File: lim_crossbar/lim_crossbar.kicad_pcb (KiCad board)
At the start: 4 copper layers, 166 x 19 mm, 13 parts, among them J1 Conn_02x12_Counter_Clockwise, J2 Conn_02x12_Counter_Clockwise, J3 Conn_02x12_Counter_Clockwise, J4 Conn_02x08_Odd_Even, J5 Conn_02x08_Odd_Even

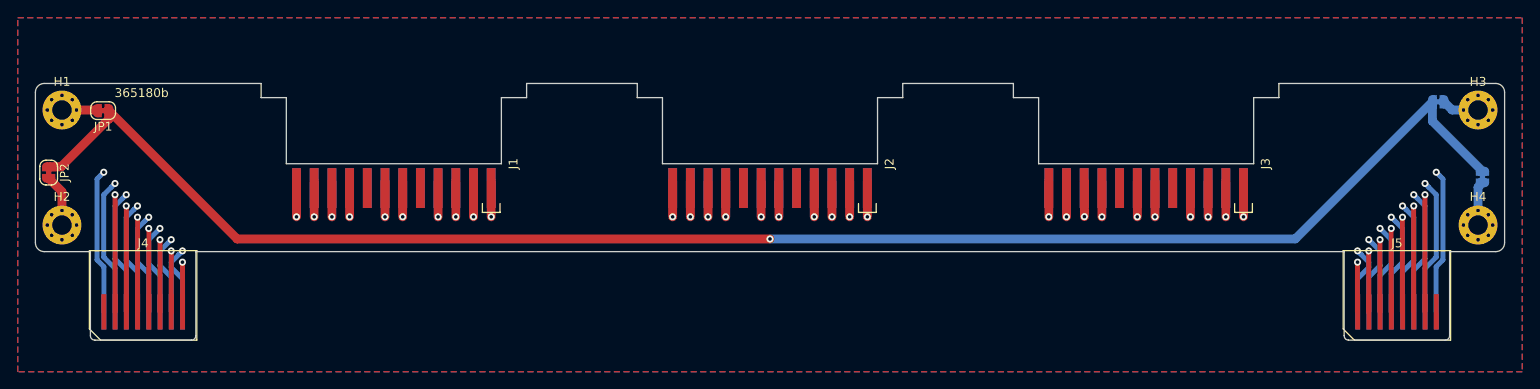
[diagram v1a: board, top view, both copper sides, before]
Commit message: otter crossbars shortened
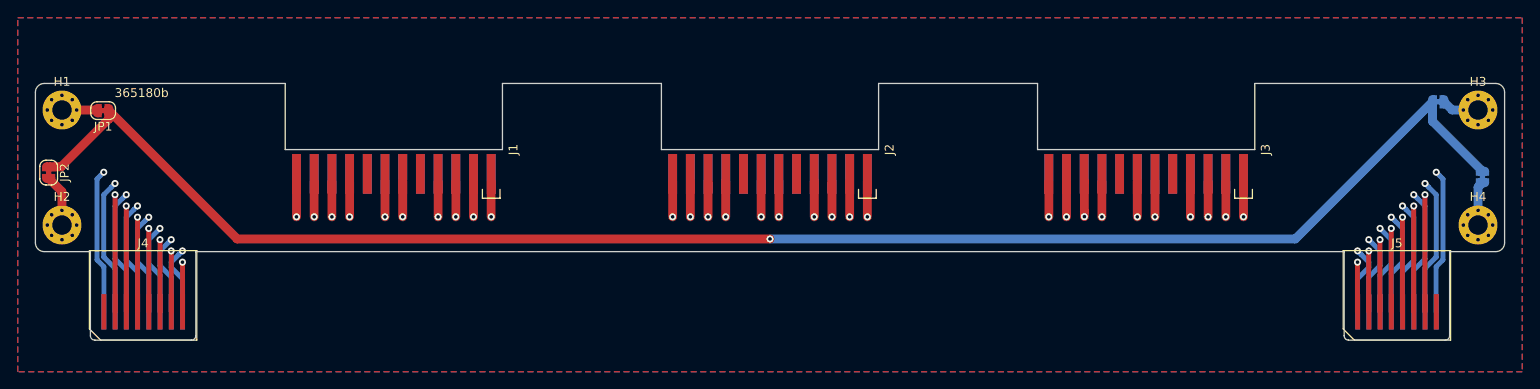
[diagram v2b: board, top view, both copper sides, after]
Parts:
- moved J1 1.60 mm to (-42.5, -21.5)
- moved J2 1.60 mm to (0.00, -21.5)
- moved J3 1.60 mm to (42.5, -21.5)
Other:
- outline, holes or cut-outs redrawn
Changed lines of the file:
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@@
-(kicad_pcb (version 20171130) (host pcbnew 5.1.5-rc1)
+(kicad_pcb (version 20171130) (host pcbnew 5.1.5)
   (general
     (thickness 1.6)
-    (drawings 33)
+    (drawings 23)
     (tracks 379)
     (zones 0)
@@
     (pad_to_mask_clearance 0.051)
     (solder_mask_min_width 0.25)
-    (aux_axis_origin 0 -21.43)
-    (grid_origin 0 -21.43)
+    (aux_axis_origin 0 -29)
+    (grid_origin 0 -29)
     (visible_elements FFFFFFFF)
     (pcbplotparams
@@
   )
   (module custom:PinSocket_2x12_P2.00mm_Vertical_EDGE (layer F.Cu)
-    (at 0 -19.93)
+    (at 0 -21.53)
     (descr "edge-mounted straight socket strip, 2x12, 2.00mm pitch, double cols (from Kicad 4.0.7), SQT-112-03-L-D")
     (tags "Edge mounted socket strip EDGE 2x12 2.00mm double row")
@@
     (fp_line (start 12 5.5) (end 10 5.5) (layer F.SilkS) (width 0.15))
     (fp_line (start 12 4.5) (end 12 5.5) (layer F.SilkS) (width 0.15))
-    (fp_line (start 12.15 0) (end -12.15 0) (layer Edge.Cuts) (width 0.12))
+    (fp_line (start 12.27 0) (end -12.27 0) (layer Edge.Cuts) (width 0.12))
     (fp_line (start 12.15 0.25) (end -12.15 0.25) (layer B.Fab) (width 0.12))
     (fp_line (start 12.15 0.25) (end -12.15 0.25) (layer F.Fab) (width 0.12))
@@
   )
   (module custom:PinSocket_2x12_P2.00mm_Vertical_EDGE (layer F.Cu)
-    (at -42.5 -19.93)
+    (at -42.5 -21.53)
     (descr "edge-mounted straight socket strip, 2x12, 2.00mm pitch, double cols (from Kicad 4.0.7), SQT-112-03-L-D")
     (tags "Edge mounted socket strip EDGE 2x12 2.00mm double row")
@@
     (fp_line (start 12 5.5) (end 10 5.5) (layer F.SilkS) (width 0.15))
     (fp_line (start 12 4.5) (end 12 5.5) (layer F.SilkS) (width 0.15))
-    (fp_line (start 12.15 0) (end -12.15 0) (layer Edge.Cuts) (width 0.12))
+    (fp_line (start 12.27 0) (end -12.27 0) (layer Edge.Cuts) (width 0.12))
     (fp_line (start 12.15 0.25) (end -12.15 0.25) (layer B.Fab) (width 0.12))
     (fp_line (start 12.15 0.25) (end -12.15 0.25) (layer F.Fab) (width 0.12))
@@
   )
   (module custom:PinSocket_2x12_P2.00mm_Vertical_EDGE (layer F.Cu)
-    (at 42.5 -19.93)
+    (at 42.5 -21.53)
     (descr "edge-mounted straight socket strip, 2x12, 2.00mm pitch, double cols (from Kicad 4.0.7), SQT-112-03-L-D")
     (tags "Edge mounted socket strip EDGE 2x12 2.00mm double row")
@@
     (fp_line (start 12 5.5) (end 10 5.5) (layer F.SilkS) (width 0.15))
     (fp_line (start 12 4.5) (end 12 5.5) (layer F.SilkS) (width 0.15))
-    (fp_line (start 12.15 0) (end -12.15 0) (layer Edge.Cuts) (width 0.12))
+    (fp_line (start 12.27 0) (end -12.27 0) (layer Edge.Cuts) (width 0.12))
     (fp_line (start 12.15 0.25) (end -12.15 0.25) (layer B.Fab) (width 0.12))
     (fp_line (start 12.15 0.25) (end -12.15 0.25) (layer F.Fab) (width 0.12))
@@
       ))
   )
+  (gr_line (start 54.77 -21.53) (end 54.77 -29) (layer Edge.Cuts) (width 0.05))
+  (gr_line (start 30.23 -21.53) (end 30.23 -29) (layer Edge.Cuts) (width 0.05))
+  (gr_line (start 12.27 -21.53) (end 12.27 -29) (layer Edge.Cuts) (width 0.05))
+  (gr_line (start -30.23 -21.53) (end -30.23 -29) (layer Edge.Cuts) (width 0.05))
+  (gr_line (start -54.77 -21.53) (end -54.77 -29) (layer Edge.Cuts) (width 0.05))
+  (gr_line (start -12.27 -29) (end -30.23 -29) (layer Edge.Cuts) (width 0.05))
+  (gr_line (start -12.27 -21.53) (end -12.27 -29) (layer Edge.Cuts) (width 0.05))
+  (gr_line (start -87 2.5) (end 89 2.5) (layer Dwgs.User) (width 0.15))
+  (gr_line (start -87 -9.5) (end 89 -9.5) (layer Dwgs.User) (width 0.15))
   (gr_text 365180b (at -71 -27.93) (layer B.SilkS)
     (effects (font (size 1 1) (thickness 0.15)) (justify mirror))
@@
   (gr_arc (start 82 -11) (end 82 -10) (angle -90) (layer Edge.Cuts) (width 0.05))
   (gr_line (start 83 -11) (end 83 -28) (layer Edge.Cuts) (width 0.05))
-  (gr_line (start -57.5 -29) (end -82 -29) (layer Edge.Cuts) (width 0.05))
-  (gr_line (start -15 -29) (end -27.5 -29) (layer Edge.Cuts) (width 0.05))
-  (gr_line (start 27.5 -29) (end 15 -29) (layer Edge.Cuts) (width 0.05))
-  (gr_line (start 82 -29) (end 57.5 -29) (layer Edge.Cuts) (width 0.05))
-  (gr_line (start -30.35 -27.4) (end -27.5 -27.4) (layer Edge.Cuts) (width 0.05))
-  (gr_line (start -54.65 -19.93) (end -54.65 -27.4) (layer Edge.Cuts) (width 0.05))
-  (gr_line (start -27.5 -27.4) (end -27.5 -29) (layer Edge.Cuts) (width 0.05))
-  (gr_line (start -30.35 -19.93) (end -30.35 -27.4) (layer Edge.Cuts) (width 0.05))
-  (gr_line (start -57.5 -27.4) (end -57.5 -29) (layer Edge.Cuts) (width 0.05))
-  (gr_line (start -57.5 -27.4) (end -54.65 -27.4) (layer Edge.Cuts) (width 0.05))
-  (gr_line (start 54.65 -27.4) (end 57.5 -27.4) (layer Edge.Cuts) (width 0.05))
-  (gr_line (start 30.35 -19.93) (end 30.35 -27.4) (layer Edge.Cuts) (width 0.05))
-  (gr_line (start 57.5 -27.4) (end 57.5 -29) (layer Edge.Cuts) (width 0.05))
-  (gr_line (start 54.65 -19.93) (end 54.65 -27.4) (layer Edge.Cuts) (width 0.05))
-  (gr_line (start 27.5 -27.4) (end 27.5 -29) (layer Edge.Cuts) (width 0.05))
-  (gr_line (start 27.5 -27.4) (end 30.35 -27.4) (layer Edge.Cuts) (width 0.05))
-  (gr_line (start -15 -27.4) (end -15 -29) (layer Edge.Cuts) (width 0.05))
-  (gr_line (start 15 -27.4) (end 15 -29) (layer Edge.Cuts) (width 0.05))
-  (gr_line (start 12.15 -27.4) (end 15 -27.4) (layer Edge.Cuts) (width 0.05))
-  (gr_line (start 12.15 -19.93) (end 12.15 -27.4) (layer Edge.Cuts) (width 0.05))
-  (gr_line (start -15 -27.4) (end -12.15 -27.4) (layer Edge.Cuts) (width 0.05))
-  (gr_line (start -12.15 -19.93) (end -12.15 -27.4) (layer Edge.Cuts) (width 0.05))
+  (gr_line (start -54.77 -29) (end -82 -29) (layer Edge.Cuts) (width 0.05))
+  (gr_line (start 30.23 -29) (end 12.27 -29) (layer Edge.Cuts) (width 0.05))
+  (gr_line (start 82 -29) (end 54.77 -29) (layer Edge.Cuts) (width 0.05))
   (gr_arc (start 82 -28) (end 83 -28) (angle -90) (layer Edge.Cuts) (width 0.05))
   (gr_arc (start -82 -28) (end -82 -29) (angle -90) (layer Edge.Cuts) (width 0.05))

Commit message: update silk
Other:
- board text added: "6c4861d"
- board text removed: "365180b"
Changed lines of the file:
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@@
       (padsonsilk false)
       (subtractmaskfromsilk false)
-      (outputformat 3)
+      (outputformat 1)
       (mirror false)
       (drillshape 0)
@@
   (gr_line (start -87 2.5) (end 89 2.5) (layer Dwgs.User) (width 0.15))
   (gr_line (start -87 -9.5) (end 89 -9.5) (layer Dwgs.User) (width 0.15))
-  (gr_text 365180b (at -71 -27.93) (layer B.SilkS)
+  (gr_text 6c4861d (at -71 -27.93) (layer B.SilkS)
     (effects (font (size 1 1) (thickness 0.15)) (justify mirror))
   )
-  (gr_text 365180b (at -71 -27.93) (layer F.SilkS)
+  (gr_text 6c4861d (at -71 -27.93) (layer F.SilkS)
     (effects (font (size 1 1) (thickness 0.15)))
   )

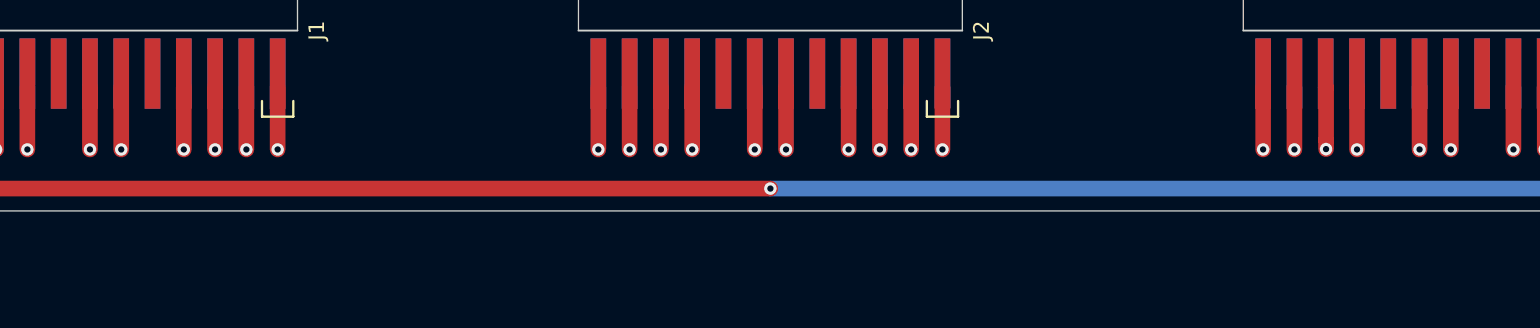
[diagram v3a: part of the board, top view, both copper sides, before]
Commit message: fix lim baseboard bug
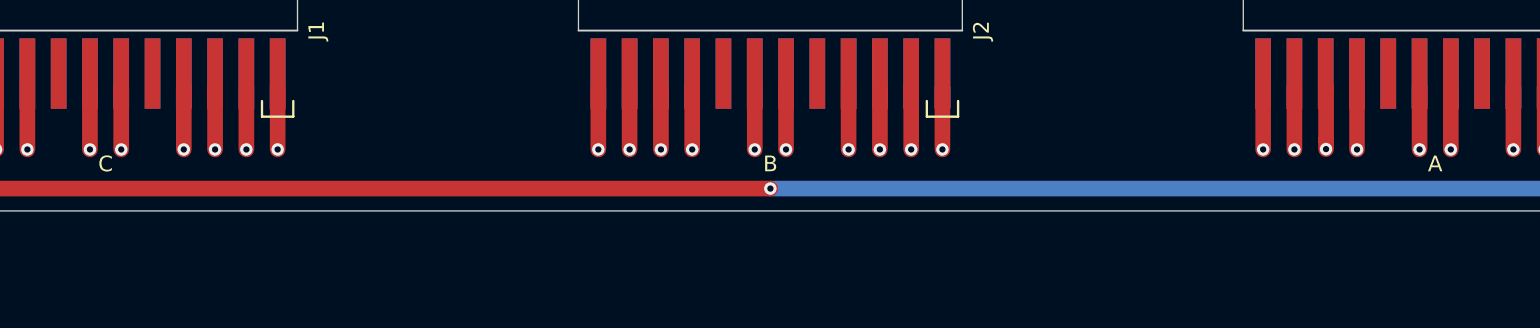
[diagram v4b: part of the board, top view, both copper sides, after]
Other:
- board text added: "A"
- board text added: "B"
- board text added: "C"
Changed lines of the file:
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@@
   (general
     (thickness 1.6)
-    (drawings 23)
+    (drawings 29)
     (tracks 379)
     (zones 0)
@@
       ))
   )
+  (gr_text C (at -42.5 -13) (layer B.SilkS)
+    (effects (font (size 1 1) (thickness 0.15)) (justify mirror))
+  )
+  (gr_text C (at -42.5 -13) (layer F.SilkS)
+    (effects (font (size 1 1) (thickness 0.15)))
+  )
+  (gr_text B (at 0 -13) (layer B.SilkS)
+    (effects (font (size 1 1) (thickness 0.15)) (justify mirror))
+  )
+  (gr_text B (at 0 -13) (layer F.SilkS)
+    (effects (font (size 1 1) (thickness 0.15)))
+  )
+  (gr_text A (at 42.5 -13) (layer B.SilkS)
+    (effects (font (size 1 1) (thickness 0.15)) (justify mirror))
+  )
+  (gr_text A (at 42.5 -13) (layer F.SilkS)
+    (effects (font (size 1 1) (thickness 0.15)))
+  )
   (gr_line (start 54.77 -21.53) (end 54.77 -29) (layer Edge.Cuts) (width 0.05))
